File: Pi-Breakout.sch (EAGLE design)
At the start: 43 parts, among them CON1 RPI-ZERO, CON2 RPI-ZERO, J1 2X1-LOCKING, J2 2X1-LOCKING, U1 TC1014-3.3V, U2 TC1014-3.3V

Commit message: Added Second CIRCUIT
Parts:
- removed 3V3-OUT1: (no value), adafruit:PINHD-1X3
- removed DIG_V: 2X2HEADER, HappyBrackets:2X2HEADER
- added J3: 1X2EDGE, HappyBrackets:1X2EDGE
- added U$1: 1X3EDGE, HappyBrackets:1X3EDGE
- J2: value 2X1-LOCKING -> 1X2EDGE; device HappyBrackets:2X1-LOCKING -> HappyBrackets:1X2EDGE
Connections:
- net ANA_GND: now also U$1.2; no longer 3V3-OUT1.2
- net AN_5V: now also U$1.3; no longer 3V3-OUT1.1
- net DIG_5V: now also J3.1; no longer DIG_V.3, DIG_V.4
- net DIG_GND: now also J3.2; no longer DIG_V.1, DIG_V.2
- net N$42: now also U$1.1; no longer 3V3-OUT1.3
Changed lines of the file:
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@@
 <part name="C1" library="rcl" library_urn="urn:adsk.eagle:library:334" deviceset="C-EU" device="C0603" package3d_urn="urn:adsk.eagle:package:23616/2" value="470p"/>
 <part name="C2" library="rcl" library_urn="urn:adsk.eagle:library:334" deviceset="C-EU" device="C0603" package3d_urn="urn:adsk.eagle:package:23616/2" value="1uF"/>
-<part name="J2" library="HappyBrackets" library_urn="urn:adsk.eagle:library:5224691" deviceset="2X1-LOCKING" device=""/>
+<part name="J2" library="HappyBrackets" library_urn="urn:adsk.eagle:library:5224691" deviceset="1X2EDGE" device=""/>
 <part name="L9" library="HappyBrackets" library_urn="urn:adsk.eagle:library:5224691" deviceset="BLM31A" device="" package3d_urn="urn:adsk.eagle:package:15829/1"/>
 <part name="L10" library="HappyBrackets" library_urn="urn:adsk.eagle:library:5224691" deviceset="BLM31A" device="" package3d_urn="urn:adsk.eagle:package:15829/1"/>
@@
 <part name="L12" library="HappyBrackets" library_urn="urn:adsk.eagle:library:5224691" deviceset="BLM31A" device="" package3d_urn="urn:adsk.eagle:package:15829/1"/>
 <part name="U2" library="HappyBrackets" library_urn="urn:adsk.eagle:library:5224691" deviceset="TC1014-3.3V" device="" package3d_urn="urn:adsk.eagle:package:6644337/2"/>
-<part name="3V3-OUT1" library="adafruit" deviceset="PINHD-1X3" device=""/>
 <part name="C3" library="rcl" library_urn="urn:adsk.eagle:library:334" deviceset="C-EU" device="C0603" package3d_urn="urn:adsk.eagle:package:23616/2" value="470p"/>
 <part name="C4" library="rcl" library_urn="urn:adsk.eagle:library:334" deviceset="C-EU" device="C0603" package3d_urn="urn:adsk.eagle:package:23616/2" value="1uF"/>
 <part name="C5" library="rcl" library_urn="urn:adsk.eagle:library:334" deviceset="C-EU" device="C0603" package3d_urn="urn:adsk.eagle:package:23616/2" value="1uF"/>
 <part name="C6" library="rcl" library_urn="urn:adsk.eagle:library:334" deviceset="C-EU" device="C0603" package3d_urn="urn:adsk.eagle:package:23616/2" value="1uF"/>
-<part name="DIG_V" library="HappyBrackets" library_urn="urn:adsk.eagle:library:5224691" deviceset="2X2HEADER" device=""/>
+<part name="J3" library="HappyBrackets" library_urn="urn:adsk.eagle:library:5224691" deviceset="1X2EDGE" device=""/>
+<part name="U$1" library="HappyBrackets" library_urn="urn:adsk.eagle:library:5224691" deviceset="1X3EDGE" device=""/>
 </parts>
 <sheets>
@@
 <instance part="L12" gate="G$1" x="-111.76" y="-12.7"/>
 <instance part="U2" gate="G$1" x="-30.48" y="-38.1"/>
-<instance part="3V3-OUT1" gate="A" x="-58.42" y="2.54" rot="R90"/>
 <instance part="C3" gate="G$1" x="-35.56" y="-27.94"/>
 <instance part="C4" gate="G$1" x="-30.48" y="-17.78"/>
 <instance part="C5" gate="G$1" x="-83.82" y="-12.7"/>
 <instance part="C6" gate="G$1" x="-147.32" y="-17.78"/>
-<instance part="DIG_V" gate="G$1" x="-167.64" y="-15.24" rot="R180"/>
+<instance part="J3" gate="G$1" x="-165.1" y="-20.32" rot="MR0"/>
+<instance part="U$1" gate="G$1" x="-58.42" y="0" rot="MR90"/>
 </instances>
 <busses>
@@
 <net name="AN_5V" class="0">
 <segment>
-<pinref part="3V3-OUT1" gate="A" pin="1"/>
 <pinref part="U2" gate="G$1" pin="VIN"/>
-<wire x1="-60.96" y1="0" x2="-68.58" y2="0" width="0.1524" layer="91"/>
-<wire x1="-68.58" y1="0" x2="-68.58" y2="-15.24" width="0.1524" layer="91"/>
+<wire x1="-68.58" y1="0" x2="-68.58" y2="-2.54" width="0.1524" layer="91"/>
 <pinref part="U2" gate="G$1" pin="_SHDN"/>
+<wire x1="-68.58" y1="-2.54" x2="-68.58" y2="-15.24" width="0.1524" layer="91"/>
 <wire x1="-68.58" y1="-25.4" x2="-73.66" y2="-25.4" width="0.1524" layer="91"/>
 <wire x1="-73.66" y1="-25.4" x2="-73.66" y2="-7.62" width="0.1524" layer="91"/>
 <wire x1="-73.66" y1="-7.62" x2="-73.66" y2="0" width="0.1524" layer="91"/>
 <wire x1="-73.66" y1="0" x2="-68.58" y2="0" width="0.1524" layer="91"/>
-<junction x="-68.58" y="0"/>
 <pinref part="L12" gate="G$1" pin="1"/>
 <wire x1="-111.76" y1="-5.08" x2="-83.82" y2="-5.08" width="0.1524" layer="91"/>
@@
 <wire x1="-83.82" y1="-10.16" x2="-83.82" y2="-5.08" width="0.1524" layer="91"/>
 <junction x="-83.82" y="-5.08"/>
+<pinref part="U$1" gate="G$1" pin="3"/>
+<wire x1="-60.96" y1="-2.54" x2="-68.58" y2="-2.54" width="0.1524" layer="91"/>
+<junction x="-68.58" y="-2.54"/>
 </segment>
 </net>
 <net name="N$42" class="0">
 <segment>
-<pinref part="3V3-OUT1" gate="A" pin="3"/>
-<wire x1="-55.88" y1="0" x2="-55.88" y2="-7.62" width="0.1524" layer="91"/>
 <wire x1="-55.88" y1="-7.62" x2="-35.56" y2="-7.62" width="0.1524" layer="91"/>
 <pinref part="U2" gate="G$1" pin="VOUT"/>
@@
 <wire x1="-35.56" y1="-15.24" x2="-30.48" y2="-15.24" width="0.1524" layer="91"/>
 <junction x="-35.56" y="-15.24"/>
+<pinref part="U$1" gate="G$1" pin="1"/>
+<wire x1="-55.88" y1="-7.62" x2="-55.88" y2="-2.54" width="0.1524" layer="91"/>
 </segment>
 </net>
@@
 <wire x1="-68.58" y1="-20.32" x2="-71.12" y2="-20.32" width="0.1524" layer="91"/>
 <wire x1="-71.12" y1="-20.32" x2="-71.12" y2="-7.62" width="0.1524" layer="91"/>
-<pinref part="3V3-OUT1" gate="A" pin="2"/>
-<wire x1="-58.42" y1="0" x2="-58.42" y2="-7.62" width="0.1524" layer="91"/>
 <wire x1="-58.42" y1="-7.62" x2="-71.12" y2="-7.62" width="0.1524" layer="91"/>
 <wire x1="-71.12" y1="-20.32" x2="-71.12" y2="-33.02" width="0.1524" layer="91"/>
@@
 <wire x1="-83.82" y1="-17.78" x2="-83.82" y2="-43.18" width="0.1524" layer="91"/>
 <junction x="-83.82" y="-43.18"/>
+<pinref part="U$1" gate="G$1" pin="2"/>
+<wire x1="-58.42" y1="-2.54" x2="-58.42" y2="-7.62" width="0.1524" layer="91"/>
 </segment>
 </net>
@@
 <wire x1="-147.32" y1="-5.08" x2="-147.32" y2="-15.24" width="0.1524" layer="91"/>
 <label x="-139.7" y="-5.08" size="1.778" layer="95"/>
-<pinref part="DIG_V" gate="G$1" pin="4"/>
-<pinref part="DIG_V" gate="G$1" pin="3"/>
-<wire x1="-177.8" y1="-17.78" x2="-157.48" y2="-17.78" width="0.1524" layer="91"/>
 <wire x1="-157.48" y1="-17.78" x2="-152.4" y2="-17.78" width="0.1524" layer="91"/>
 <wire x1="-152.4" y1="-17.78" x2="-152.4" y2="-5.08" width="0.1524" layer="91"/>
-<junction x="-157.48" y="-17.78"/>
 <wire x1="-152.4" y1="-5.08" x2="-147.32" y2="-5.08" width="0.1524" layer="91"/>
 <junction x="-147.32" y="-5.08"/>
+<pinref part="J3" gate="G$1" pin="1"/>
+<wire x1="-157.48" y1="-17.78" x2="-160.02" y2="-17.78" width="0.1524" layer="91"/>
 </segment>
 </net>
@@
 <wire x1="-147.32" y1="-43.18" x2="-144.78" y2="-43.18" width="0.1524" layer="91"/>
 <label x="-139.7" y="-43.18" size="1.778" layer="95"/>
-<pinref part="DIG_V" gate="G$1" pin="2"/>
-<pinref part="DIG_V" gate="G$1" pin="1"/>
 <wire x1="-144.78" y1="-43.18" x2="-121.92" y2="-43.18" width="0.1524" layer="91"/>
-<wire x1="-177.8" y1="-20.32" x2="-157.48" y2="-20.32" width="0.1524" layer="91"/>
 <wire x1="-157.48" y1="-20.32" x2="-154.94" y2="-20.32" width="0.1524" layer="91"/>
 <wire x1="-154.94" y1="-20.32" x2="-154.94" y2="-43.18" width="0.1524" layer="91"/>
-<junction x="-157.48" y="-20.32"/>
 <wire x1="-154.94" y1="-43.18" x2="-144.78" y2="-43.18" width="0.1524" layer="91"/>
 <junction x="-144.78" y="-43.18"/>
-</segment>
-</net>
+<pinref part="J3" gate="G$1" pin="2"/>
+<wire x1="-160.02" y1="-20.32" x2="-157.48" y2="-20.32" width="0.1524" layer="91"/>
+</segment>
+</net>

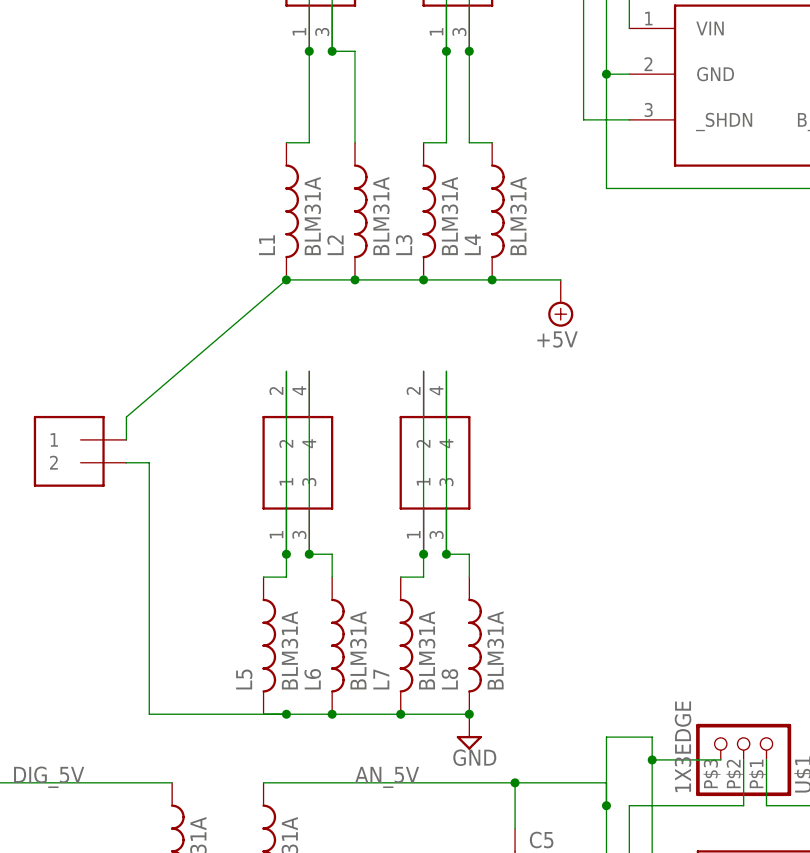
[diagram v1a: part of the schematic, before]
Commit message: Added Breakout
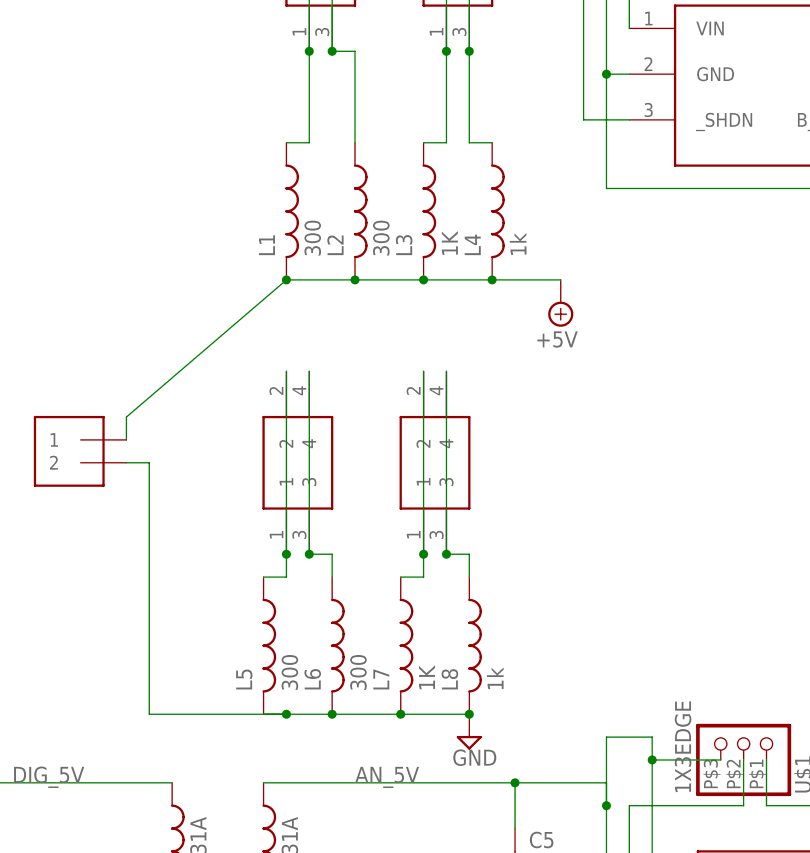
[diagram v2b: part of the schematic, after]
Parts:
- L1, L2, L5, L6: value BLM31A -> 300
- L3, L7: value BLM31A -> 1K
- L4, L8: value BLM31A -> 1k
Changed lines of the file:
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@@
 <part name="G-9" library="adafruit" deviceset="PINHD-1X3" device=""/>
 <part name="3V-17" library="adafruit" deviceset="PINHD-1X3" device=""/>
-<part name="L1" library="HappyBrackets" library_urn="urn:adsk.eagle:library:5224691" deviceset="BLM31A" device="" package3d_urn="urn:adsk.eagle:package:15829/1"/>
-<part name="L2" library="HappyBrackets" library_urn="urn:adsk.eagle:library:5224691" deviceset="BLM31A" device="" package3d_urn="urn:adsk.eagle:package:15829/1"/>
-<part name="L3" library="HappyBrackets" library_urn="urn:adsk.eagle:library:5224691" deviceset="BLM31A" device="" package3d_urn="urn:adsk.eagle:package:15829/1"/>
-<part name="L4" library="HappyBrackets" library_urn="urn:adsk.eagle:library:5224691" deviceset="BLM31A" device="" package3d_urn="urn:adsk.eagle:package:15829/1"/>
-<part name="L5" library="HappyBrackets" library_urn="urn:adsk.eagle:library:5224691" deviceset="BLM31A" device="" package3d_urn="urn:adsk.eagle:package:15829/1"/>
-<part name="L6" library="HappyBrackets" library_urn="urn:adsk.eagle:library:5224691" deviceset="BLM31A" device="" package3d_urn="urn:adsk.eagle:package:15829/1"/>
-<part name="L7" library="HappyBrackets" library_urn="urn:adsk.eagle:library:5224691" deviceset="BLM31A" device="" package3d_urn="urn:adsk.eagle:package:15829/1"/>
-<part name="L8" library="HappyBrackets" library_urn="urn:adsk.eagle:library:5224691" deviceset="BLM31A" device="" package3d_urn="urn:adsk.eagle:package:15829/1"/>
+<part name="L1" library="HappyBrackets" library_urn="urn:adsk.eagle:library:5224691" deviceset="BLM31A" device="" package3d_urn="urn:adsk.eagle:package:15829/1" value="300"/>
+<part name="L2" library="HappyBrackets" library_urn="urn:adsk.eagle:library:5224691" deviceset="BLM31A" device="" package3d_urn="urn:adsk.eagle:package:15829/1" value="300"/>
+<part name="L3" library="HappyBrackets" library_urn="urn:adsk.eagle:library:5224691" deviceset="BLM31A" device="" package3d_urn="urn:adsk.eagle:package:15829/1" value="1K"/>
+<part name="L4" library="HappyBrackets" library_urn="urn:adsk.eagle:library:5224691" deviceset="BLM31A" device="" package3d_urn="urn:adsk.eagle:package:15829/1" value="1k"/>
+<part name="L5" library="HappyBrackets" library_urn="urn:adsk.eagle:library:5224691" deviceset="BLM31A" device="" package3d_urn="urn:adsk.eagle:package:15829/1" value="300"/>
+<part name="L6" library="HappyBrackets" library_urn="urn:adsk.eagle:library:5224691" deviceset="BLM31A" device="" package3d_urn="urn:adsk.eagle:package:15829/1" value="300"/>
+<part name="L7" library="HappyBrackets" library_urn="urn:adsk.eagle:library:5224691" deviceset="BLM31A" device="" package3d_urn="urn:adsk.eagle:package:15829/1" value="1K"/>
+<part name="L8" library="HappyBrackets" library_urn="urn:adsk.eagle:library:5224691" deviceset="BLM31A" device="" package3d_urn="urn:adsk.eagle:package:15829/1" value="1k"/>
 <part name="SUPPLY1" library="supply2" library_urn="urn:adsk.eagle:library:372" deviceset="GND" device=""/>
 <part name="SUPPLY2" library="supply2" library_urn="urn:adsk.eagle:library:372" deviceset="+5V" device=""/>
